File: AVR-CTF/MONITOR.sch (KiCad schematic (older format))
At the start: 13 parts

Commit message: Esquematico para revision
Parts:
- gave numbers to parts that had none: 13
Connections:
- net VDD renamed +3V3
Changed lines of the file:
@@
 $EndDescr
 $Comp
-L RF_Module:ESP32-WROOM-32D U?
+L RF_Module:ESP32-WROOM-32D U3
 U 1 1 621CC162
 P 1800 2350
-F 0 "U?" H 2300 900 50  0000 C CNN
+F 0 "U3" H 2300 900 50  0000 C CNN
 F 1 "ESP32-WROOM-32D" H 2300 1000 50  0000 C CNN
 F 2 "RF_Module:ESP32-WROOM-32" H 1800 850 50  0001 C CNN
@@
 $EndComp
 $Comp
-L Device:C C?
+L Device:C C6
 U 1 1 621D2118
 P 3400 950
-F 0 "C?" H 3515 996 50  0000 L CNN
+F 0 "C6" H 3515 996 50  0000 L CNN
 F 1 "10uF" H 3515 905 50  0000 L CNN
 F 2 "Capacitor_SMD:C_0805_2012Metric_Pad1.18x1.45mm_HandSolder" H 3438 800 50  0001 C CNN
@@
 $EndComp
 $Comp
-L Device:C C?
+L Device:C C7
 U 1 1 621D24F4
 P 3800 950
-F 0 "C?" H 3915 996 50  0000 L CNN
+F 0 "C7" H 3915 996 50  0000 L CNN
 F 1 "1uF" H 3915 905 50  0000 L CNN
 F 2 "Capacitor_SMD:C_0603_1608Metric_Pad1.08x0.95mm_HandSolder" H 3838 800 50  0001 C CNN
@@
 $EndComp
 $Comp
-L Device:C C?
+L Device:C C8
 U 1 1 621D2B1C
 P 4200 950
-F 0 "C?" H 4315 996 50  0000 L CNN
+F 0 "C8" H 4315 996 50  0000 L CNN
 F 1 "0.1uF" H 4315 905 50  0000 L CNN
 F 2 "Capacitor_SMD:C_0603_1608Metric_Pad1.08x0.95mm_HandSolder" H 4238 800 50  0001 C CNN
@@
 	3800 1100 4200 1100
 Connection ~ 3800 1100
-$Comp
-L power:VDD #PWR?
-U 1 1 621E240B
-P 3800 800
-F 0 "#PWR?" H 3800 650 50  0001 C CNN
-F 1 "VDD" H 3815 973 50  0000 C CNN
-F 2 "" H 3800 800 50  0001 C CNN
-F 3 "" H 3800 800 50  0001 C CNN
-	1    3800 800
-	1    0    0    -1
-$EndComp
-$Comp
-L power:VDD #PWR?
-U 1 1 621E27EB
-P 1800 900
-F 0 "#PWR?" H 1800 750 50  0001 C CNN
-F 1 "VDD" H 1815 1073 50  0000 C CNN
-F 2 "" H 1800 900 50  0001 C CNN
-F 3 "" H 1800 900 50  0001 C CNN
-	1    1800 900
-	1    0    0    -1
-$EndComp
 Wire Wire Line
 	1800 900  1800 950
 $Comp
-L power:GND #PWR?
+L power:GND #PWR017
 U 1 1 621E322C
 P 3800 1200
-F 0 "#PWR?" H 3800 950 50  0001 C CNN
+F 0 "#PWR017" H 3800 950 50  0001 C CNN
 F 1 "GND" H 3805 1027 50  0000 C CNN
 F 2 "" H 3800 1200 50  0001 C CNN
@@
 	3800 1100 3800 1200
 $Comp
-L power:GND #PWR?
+L power:GND #PWR014
 U 1 1 621E3647
 P 1800 3750
-F 0 "#PWR?" H 1800 3500 50  0001 C CNN
+F 0 "#PWR014" H 1800 3500 50  0001 C CNN
 F 1 "GND" H 1805 3577 50  0000 C CNN
 F 2 "" H 1800 3750 50  0001 C CNN
@@
 $EndComp
 $Comp
-L Device:R R?
+L Device:R R4
 U 1 1 621E4581
 P 5775 975
-F 0 "R?" H 5845 1021 50  0000 L CNN
+F 0 "R4" H 5845 1021 50  0000 L CNN
 F 1 "10K" H 5845 930 50  0000 L CNN
 F 2 "Resistor_SMD:R_0603_1608Metric_Pad0.98x0.95mm_HandSolder" V 5705 975 50  0001 C CNN
@@
 $EndComp
 $Comp
-L Device:C C?
+L Device:C C9
 U 1 1 621E49B9
 P 5775 1325
-F 0 "C?" H 5890 1371 50  0000 L CNN
+F 0 "C9" H 5890 1371 50  0000 L CNN
 F 1 "0.1uF" H 5890 1280 50  0000 L CNN
 F 2 "Capacitor_SMD:C_0603_1608Metric_Pad1.08x0.95mm_HandSolder" H 5813 1175 50  0001 C CNN
@@
 $EndComp
 $Comp
-L power:GND #PWR?
+L power:GND #PWR019
 U 1 1 621E4F01
 P 5775 1525
-F 0 "#PWR?" H 5775 1275 50  0001 C CNN
+F 0 "#PWR019" H 5775 1275 50  0001 C CNN
 F 1 "GND" H 5780 1352 50  0000 C CNN
 F 2 "" H 5775 1525 50  0001 C CNN
 F 3 "" H 5775 1525 50  0001 C CNN
 	1    5775 1525
-	1    0    0    -1
-$EndComp
-$Comp
-L power:VDD #PWR?
-U 1 1 621E53C7
-P 5775 775
-F 0 "#PWR?" H 5775 625 50  0001 C CNN
-F 1 "VDD" H 5790 948 50  0000 C CNN
-F 2 "" H 5775 775 50  0001 C CNN
-F 3 "" H 5775 775 50  0001 C CNN
-	1    5775 775
 	1    0    0    -1
 $EndComp
@@
 NoConn ~ 2400 2950
 $Comp
-L Device:R R?
+L Device:R R2
 U 1 1 6217A167
 P 1500 5500
-F 0 "R?" H 1570 5546 50  0000 L CNN
+F 0 "R2" H 1570 5546 50  0000 L CNN
 F 1 "10K" H 1570 5455 50  0000 L CNN
 F 2 "Resistor_SMD:R_0603_1608Metric_Pad0.98x0.95mm_HandSolder" V 1430 5500 50  0001 C CNN
@@
 	1500 5650 1725 5650
 $Comp
-L Device:R R?
+L Device:R R3
 U 1 1 6217B155
 P 1500 5925
-F 0 "R?" H 1325 5950 50  0000 L CNN
+F 0 "R3" H 1325 5950 50  0000 L CNN
 F 1 "10K" H 1300 5875 50  0000 L CNN
 F 2 "Resistor_SMD:R_0603_1608Metric_Pad0.98x0.95mm_HandSolder" V 1430 5925 50  0001 C CNN
@@
 	1500 5650 1250 5650
 Connection ~ 1500 5650
-$Comp
-L power:VDD #PWR?
-U 1 1 6217E4A0
-P 1500 5350
-F 0 "#PWR?" H 1500 5200 50  0001 C CNN
-F 1 "VDD" H 1515 5523 50  0000 C CNN
-F 2 "" H 1500 5350 50  0001 C CNN
-F 3 "" H 1500 5350 50  0001 C CNN
-	1    1500 5350
-	1    0    0    -1
-$EndComp
-$Comp
-L power:VDD #PWR?
-U 1 1 6217EDA0
-P 1500 6075
-F 0 "#PWR?" H 1500 5925 50  0001 C CNN
-F 1 "VDD" H 1515 6248 50  0000 C CNN
-F 2 "" H 1500 6075 50  0001 C CNN
-F 3 "" H 1500 6075 50  0001 C CNN
-	1    1500 6075
-	-1   0    0    1
-$EndComp
 Text Notes 1500 4150 0    62   ~ 0
 PROGRAMMING
@@
 EN
 $Comp
-L Device:R R?
+L Device:R R5
 U 1 1 62117B24
 P 5775 2300
-F 0 "R?" H 5845 2346 50  0000 L CNN
+F 0 "R5" H 5845 2346 50  0000 L CNN
 F 1 "10K" H 5845 2255 50  0000 L CNN
 F 2 "Resistor_SMD:R_0603_1608Metric_Pad0.98x0.95mm_HandSolder" V 5705 2300 50  0001 C CNN
@@
 $EndComp
 $Comp
-L Device:C C?
+L Device:C C10
 U 1 1 62117B2A
 P 5775 2650
-F 0 "C?" H 5890 2696 50  0000 L CNN
+F 0 "C10" H 5890 2696 50  0000 L CNN
 F 1 "0.1uF" H 5890 2605 50  0000 L CNN
 F 2 "Capacitor_SMD:C_0603_1608Metric_Pad1.08x0.95mm_HandSolder" H 5813 2500 50  0001 C CNN
@@
 $EndComp
 $Comp
-L power:GND #PWR?
+L power:GND #PWR021
 U 1 1 62117B30
 P 5775 2850
-F 0 "#PWR?" H 5775 2600 50  0001 C CNN
+F 0 "#PWR021" H 5775 2600 50  0001 C CNN
 F 1 "GND" H 5780 2677 50  0000 C CNN
 F 2 "" H 5775 2850 50  0001 C CNN
@@
 	1    0    0    -1
 $EndComp
-$Comp
-L power:VDD #PWR?
-U 1 1 62117B36
-P 5775 2100
-F 0 "#PWR?" H 5775 1950 50  0001 C CNN
-F 1 "VDD" H 5790 2273 50  0000 C CNN
-F 2 "" H 5775 2100 50  0001 C CNN
-F 3 "" H 5775 2100 50  0001 C CNN
-	1    5775 2100
-	1    0    0    -1
-$EndComp
 Wire Wire Line
 	4850 2925 4850 3000
@@
 BOOT
 $Comp
-L Connector_Generic:Conn_01x04 J?
+L Connector_Generic:Conn_01x04 J3
 U 1 1 625AE0CF
 P 1750 4625
-F 0 "J?" H 1668 4200 50  0000 C CNN
+F 0 "J3" H 1668 4200 50  0000 C CNN
 F 1 "Prog" H 1668 4291 50  0000 C CNN
 F 2 "Connector_PinHeader_2.54mm:PinHeader_1x04_P2.54mm_Vertical" H 1750 4625 50  0001 C CNN
@@
 U0-TX
 $Comp
-L power:GND #PWR?
+L power:GND #PWR015
 U 1 1 625B38C3
 P 2000 4775
-F 0 "#PWR?" H 2000 4525 50  0001 C CNN
+F 0 "#PWR015" H 2000 4525 50  0001 C CNN
 F 1 "GND" H 2005 4602 50  0000 C CNN
 F 2 "" H 2000 4775 50  0001 C CNN
@@
 NoConn ~ 1950 4425
 $Comp
-L AVR-CTF-symbols:4-1437565-2 SW?
+L AVR-CTF-symbols:4-1437565-2 SW1
 U 1 1 621FE361
 P 4950 1350
-F 0 "SW?" V 4904 1528 50  0000 L CNN
+F 0 "SW1" V 4904 1528 50  0000 L CNN
 F 1 "4-1437565-2" V 4995 1528 50  0000 L CNN
 F 2 "AVR-CTF-footprints:Push_button_FSM4JSMATR" H 4950 1350 50  0001 L BNN
@@
 $EndComp
 $Comp
-L AVR-CTF-symbols:4-1437565-2 SW?
+L AVR-CTF-symbols:4-1437565-2 SW2
 U 1 1 622014F9
 P 4950 2675
-F 0 "SW?" V 4904 2853 50  0000 L CNN
+F 0 "SW2" V 4904 2853 50  0000 L CNN
 F 1 "4-1437565-2" V 4995 2853 50  0000 L CNN
 F 2 "AVR-CTF-footprints:Push_button_FSM4JSMATR" H 4950 2675 50  0001 L BNN
@@
 	0    1    1    0
 $EndComp
+Text Label 2500 2150 0    50   ~ 0
+U2_RX
+Text Label 2500 2250 0    50   ~ 0
+U2_TX
+$Comp
+L power:+3.3V #PWR?
+U 1 1 6274E363
+P 1800 900
+AR Path="/621FA25F/6274E363" Ref="#PWR?"  Part="1"
+AR Path="/621FB334/6274E363" Ref="#PWR0101"  Part="1"
+F 0 "#PWR0101" H 1800 750 50  0001 C CNN
+F 1 "+3.3V" H 1815 1073 50  0000 C CNN
+F 2 "" H 1800 900 50  0001 C CNN
+F 3 "" H 1800 900 50  0001 C CNN
+	1    1800 900
+	1    0    0    -1
+$EndComp
+$Comp
+L power:+3.3V #PWR?
+U 1 1 6274F33F
+P 3800 800
+AR Path="/621FA25F/6274F33F" Ref="#PWR?"  Part="1"
+AR Path="/621FB334/6274F33F" Ref="#PWR0102"  Part="1"
+F 0 "#PWR0102" H 3800 650 50  0001 C CNN
+F 1 "+3.3V" H 3815 973 50  0000 C CNN
+F 2 "" H 3800 800 50  0001 C CNN
+F 3 "" H 3800 800 50  0001 C CNN
+	1    3800 800
+	1    0    0    -1
+$EndComp
+$Comp
+L power:+3.3V #PWR?
+U 1 1 6274F774
+P 5775 775
+AR Path="/621FA25F/6274F774" Ref="#PWR?"  Part="1"
+AR Path="/621FB334/6274F774" Ref="#PWR0103"  Part="1"
+F 0 "#PWR0103" H 5775 625 50  0001 C CNN
+F 1 "+3.3V" H 5790 948 50  0000 C CNN
+F 2 "" H 5775 775 50  0001 C CNN
+F 3 "" H 5775 775 50  0001 C CNN
+	1    5775 775
+	1    0    0    -1
+$EndComp
+$Comp
+L power:+3.3V #PWR?
+U 1 1 6274FF68
+P 5775 2100
+AR Path="/621FA25F/6274FF68" Ref="#PWR?"  Part="1"
+AR Path="/621FB334/6274FF68" Ref="#PWR0104"  Part="1"
+F 0 "#PWR0104" H 5775 1950 50  0001 C CNN
+F 1 "+3.3V" H 5790 2273 50  0000 C CNN
+F 2 "" H 5775 2100 50  0001 C CNN
+F 3 "" H 5775 2100 50  0001 C CNN
+	1    5775 2100
+	1    0    0    -1
+$EndComp
+$Comp
+L power:+3.3V #PWR?
+U 1 1 6275236D
+P 1500 5350
+AR Path="/621FA25F/6275236D" Ref="#PWR?"  Part="1"
+AR Path="/621FB334/6275236D" Ref="#PWR0106"  Part="1"
+F 0 "#PWR0106" H 1500 5200 50  0001 C CNN
+F 1 "+3.3V" H 1515 5523 50  0000 C CNN
+F 2 "" H 1500 5350 50  0001 C CNN
+F 3 "" H 1500 5350 50  0001 C CNN
+	1    1500 5350
+	1    0    0    -1
+$EndComp
+$Comp
+L power:+3.3V #PWR?
+U 1 1 62752CBD
+P 1500 6075
+AR Path="/621FA25F/62752CBD" Ref="#PWR?"  Part="1"
+AR Path="/621FB334/62752CBD" Ref="#PWR0107"  Part="1"
+F 0 "#PWR0107" H 1500 5925 50  0001 C CNN
+F 1 "+3.3V" H 1515 6248 50  0000 C CNN
+F 2 "" H 1500 6075 50  0001 C CNN
+F 3 "" H 1500 6075 50  0001 C CNN
+	1    1500 6075
+	-1   0    0    1
+$EndComp
 $EndSCHEMATC

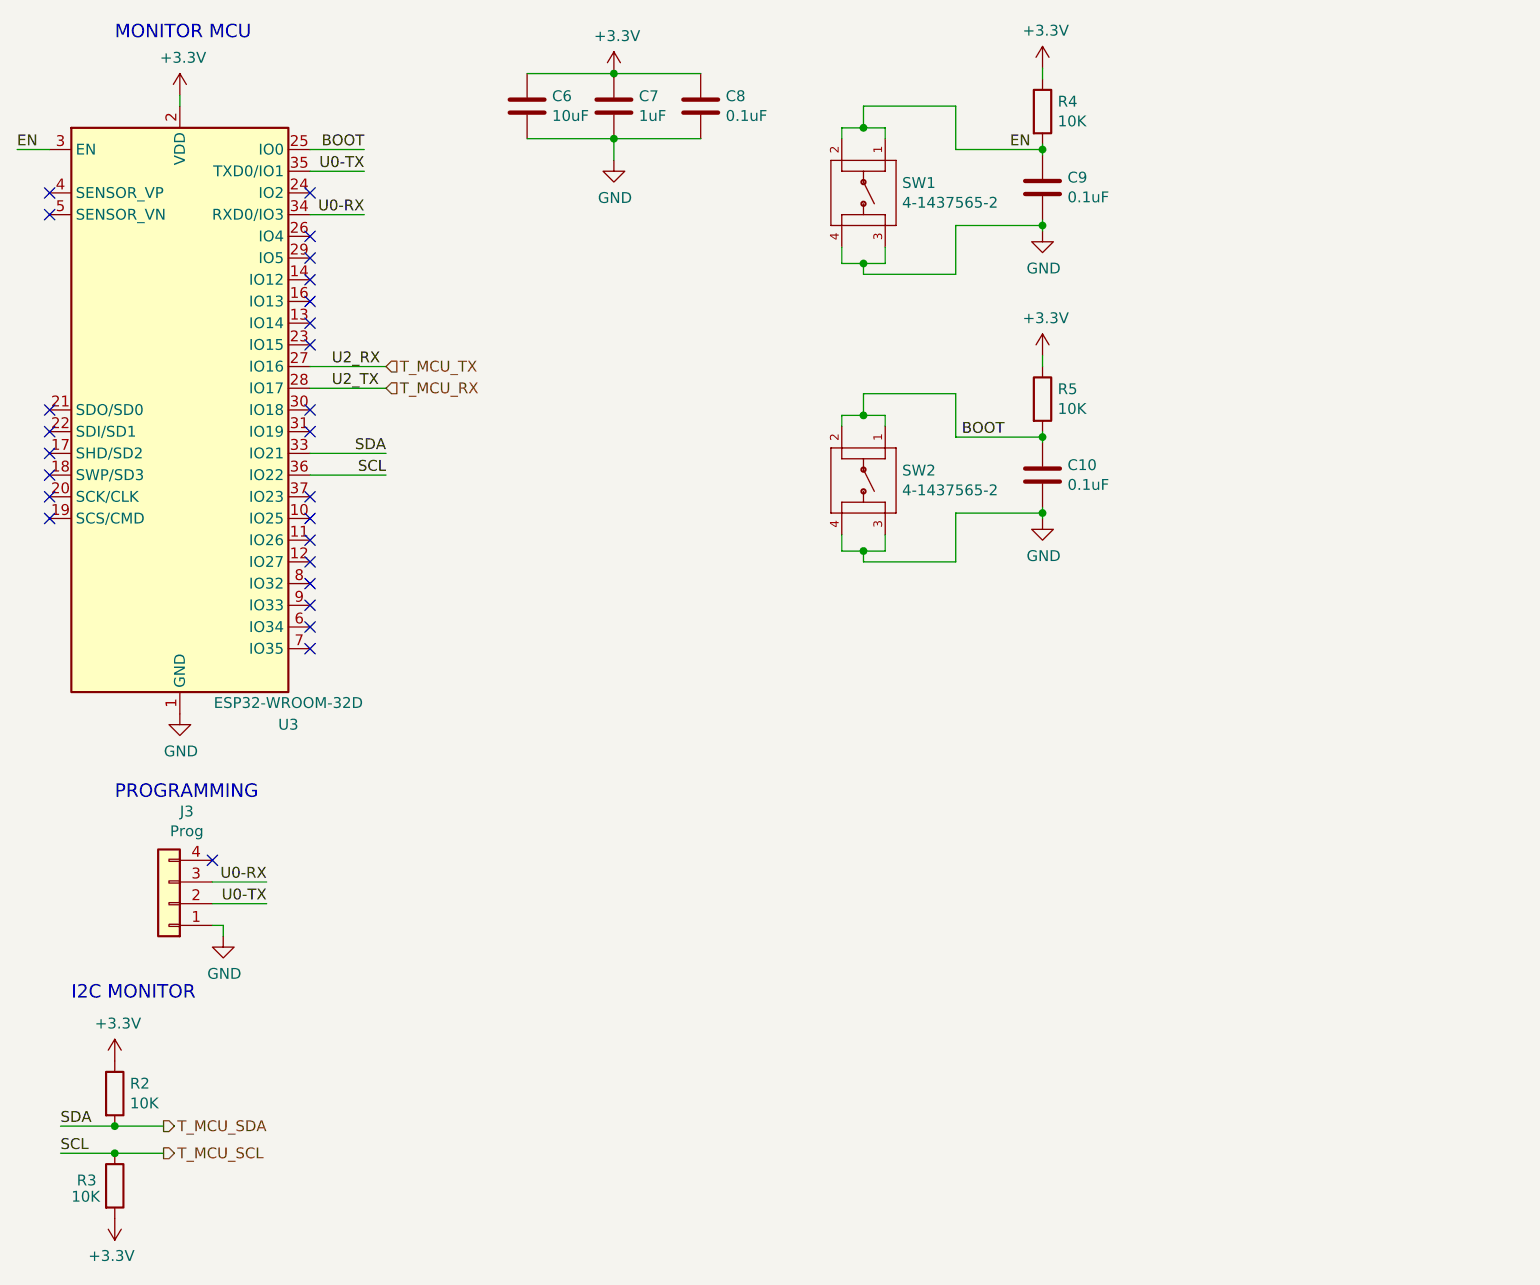
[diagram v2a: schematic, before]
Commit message: Anexo de otro FTDI y regulador de voltaje
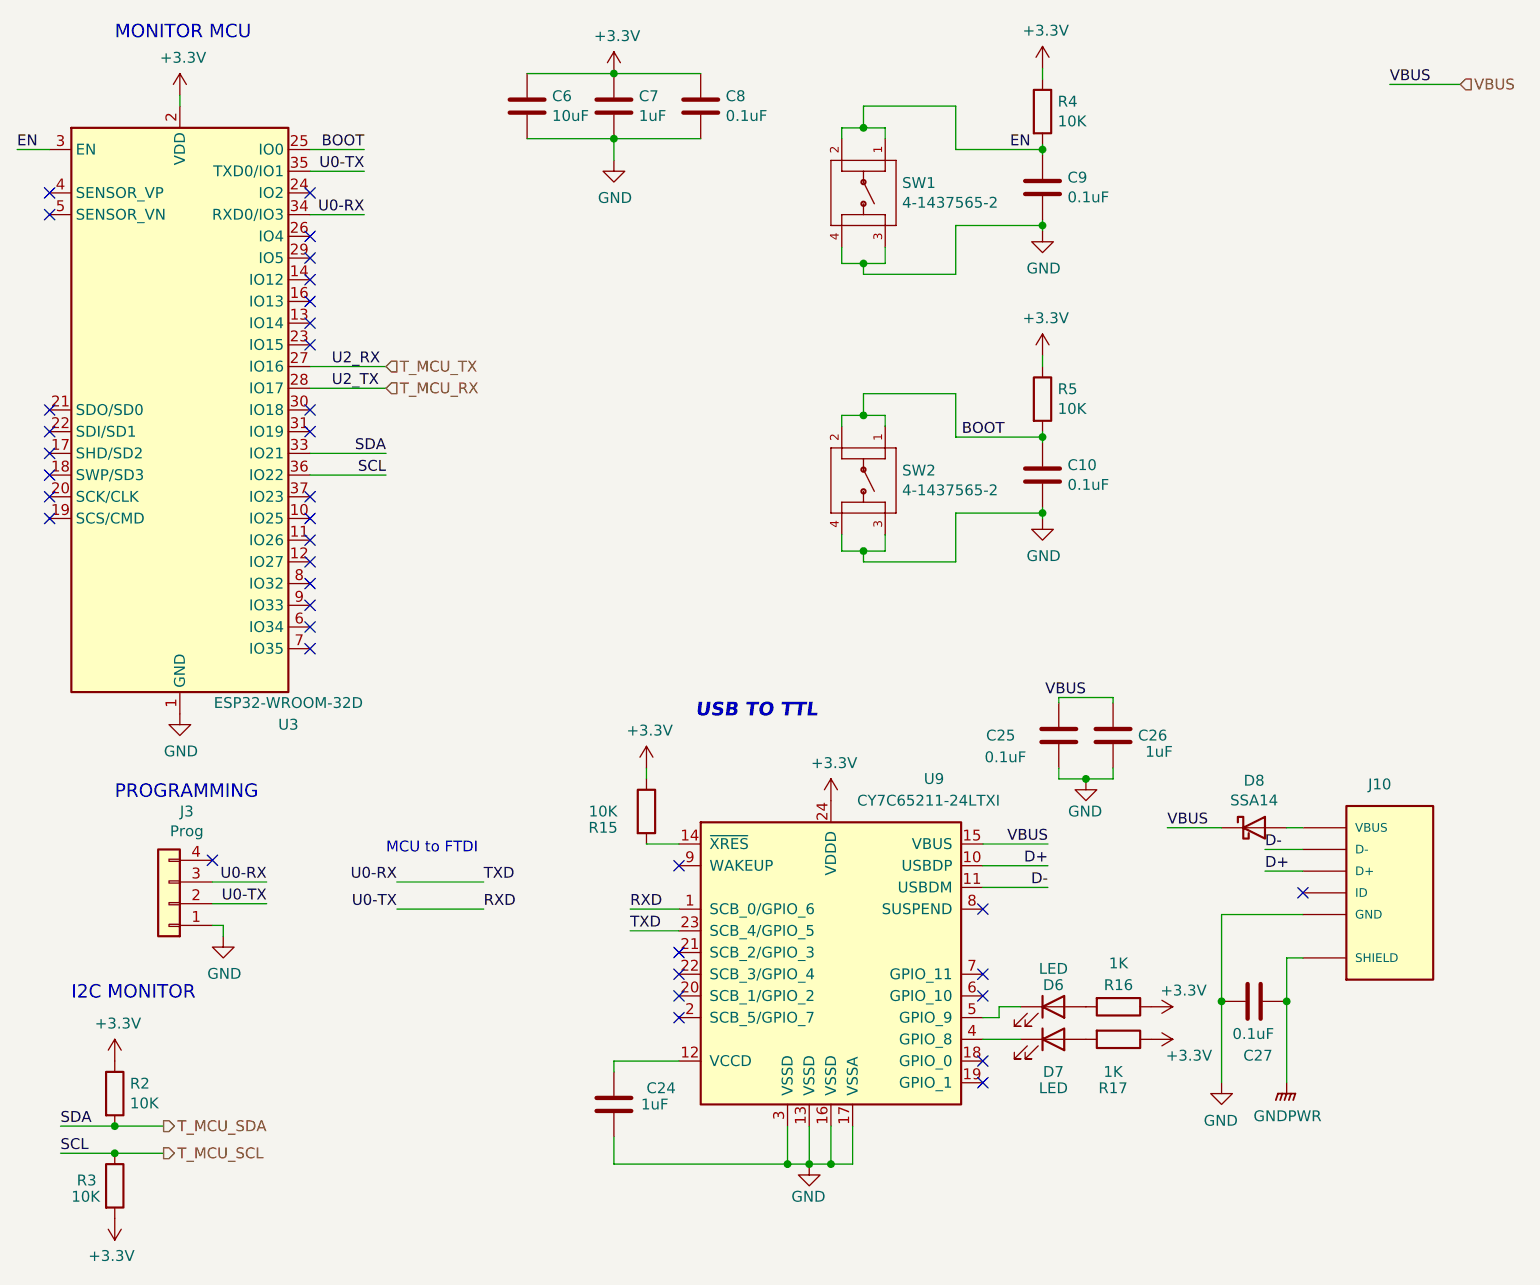
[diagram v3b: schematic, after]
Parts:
- added C24, C26: 1uF, Capacitor_SMD:C_0603_1608Metric_Pad1.08x0.95mm_HandSolder, symbol Device:C
- added C25, C27: 0.1uF, Capacitor_SMD:C_0603_1608Metric_Pad1.08x0.95mm_HandSolder, symbol Device:C
- added D6, D7: LED, LED_SMD:LED_0603_1608Metric_Pad1.05x0.95mm_HandSolder, symbol Device:LED
- added D8: SSA14, Diode_SMD:D_SMA_Handsoldering, symbol Device:D_Schottky
- added J10: USB3090-XX-X_REVE, GCT_USB3090-XX-X_REVE, symbol AVR-CTF-symbols:USB3090-XX-X_REVE
- added R15: 10K, Resistor_SMD:R_0603_1608Metric_Pad0.98x0.95mm_HandSolder, symbol Device:R
- added R16, R17: 1K, Resistor_SMD:R_0603_1608Metric_Pad0.98x0.95mm_HandSolder, symbol Device:R
- added U9: CY7C65211-24LTXI, Package_DFN_QFN:QFN-24-1EP_4x4mm_P0.5mm_EP2.6x2.6mm, symbol Interface_USB:CY7C65211-24LTXI
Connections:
- net +3V3: now also R15.1, R16.1, R17.1, U9.24 (VDDD)
- net GND: now also C24.2, C25.1, C26.1, C27.2, J10.5 (GND), U9.13 (VSSD), U9.16 (VSSD), U9.17 (VSSA), U9.3 (VSSD)
- net U0-RX renamed TXD
- net TXD: now also U9.23 (SCB_4/GPIO_5)
- net U0-TX renamed RXD
- net RXD: now also U9.1 (SCB_0/GPIO_6)
- new net: C24.1, U9.12 (VCCD)
- new net: R15.2, U9.14 (~XRES)
- new net: D7.1 (K), U9.4 (GPIO_8)
- new net: D6.1 (K), U9.5 (GPIO_9)
- new net: D8.2 (A), J10.1 (VBUS)
- new net: D7.2 (A), R17.2
- new net: D6.2 (A), R16.2
- new net D+: J10.3 (D+), U9.10 (USBDP)
- new net D-: J10.2 (D-), U9.11 (USBDM)
- new net GNDPWR: C27.1, J10.6 (SHIELD), J10.7 (SHIELD), J10.8 (SHIELD), J10.9 (SHIELD)
- new net VBUS: C25.2, C26.2, D8.1 (K), U9.15 (VBUS)
- no-connect marks 26 -> 37
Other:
- note added: "MCU to FTDI"
- note added: "USB TO TTL"

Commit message: Versión para revisión
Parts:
- J10: footprint GCT_USB3090-XX-X_REVE -> AVR-CTF-footprints:GCT_USB3090-XX-X_REVE
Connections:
- net GNDPWR renamed Earth
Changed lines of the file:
@@
 F 0 "J10" H 7275 5075 50  0000 L CNN
 F 1 "USB3090-XX-X_REVE" H 6800 5175 50  0001 L CNN
-F 2 "GCT_USB3090-XX-X_REVE" H 7375 4575 50  0001 L BNN
+F 2 "AVR-CTF-footprints:GCT_USB3090-XX-X_REVE" H 7375 4575 50  0001 L BNN
 F 3 "" H 7375 4575 50  0001 L BNN
 F 4 "GCT" H 7375 4575 50  0001 L BNN "MANUFACTURER"
@@
 F 3 "" H 6600 5450 50  0001 C CNN
 	1    6600 5450
-	1    0    0    -1
-$EndComp
-$Comp
-L power:GNDPWR #PWR?
-U 1 1 6230BCA5
-P 6900 5450
-AR Path="/6220499D/6230BCA5" Ref="#PWR?"  Part="1"
-AR Path="/621FB334/6230BCA5" Ref="#PWR060"  Part="1"
-F 0 "#PWR060" H 6900 5250 50  0001 C CNN
-F 1 "GNDPWR" H 6904 5296 50  0000 C CNN
-F 2 "" H 6900 5400 50  0001 C CNN
-F 3 "" H 6900 5400 50  0001 C CNN
-	1    6900 5450
 	1    0    0    -1
 $EndComp
@@
 Text Label 7375 850  0    50   ~ 0
 VBUS
+$Comp
+L power:Earth #PWR0108
+U 1 1 6239B255
+P 6900 5450
+F 0 "#PWR0108" H 6900 5200 50  0001 C CNN
+F 1 "Earth" H 6900 5300 50  0001 C CNN
+F 2 "" H 6900 5450 50  0001 C CNN
+F 3 "~" H 6900 5450 50  0001 C CNN
+	1    6900 5450
+	1    0    0    -1
+$EndComp
 $EndSCHEMATC

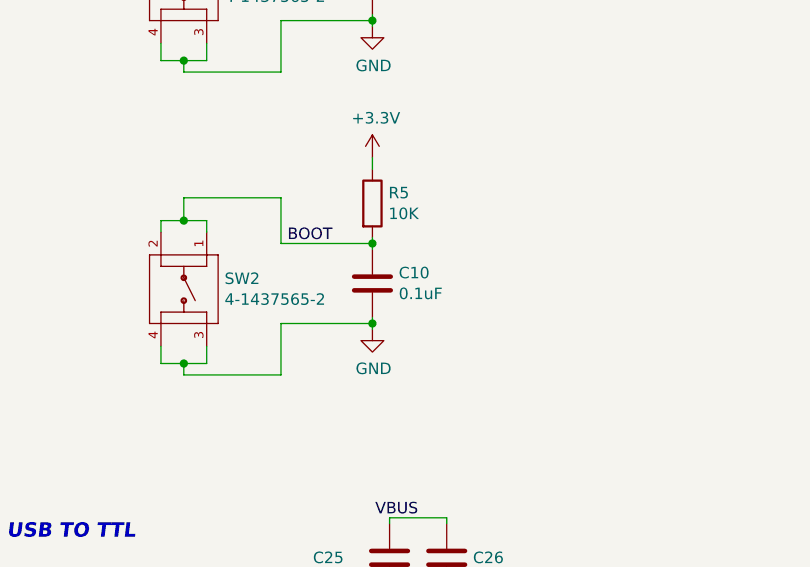
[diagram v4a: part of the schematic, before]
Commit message: Generacion de gerbers y boom agrupado
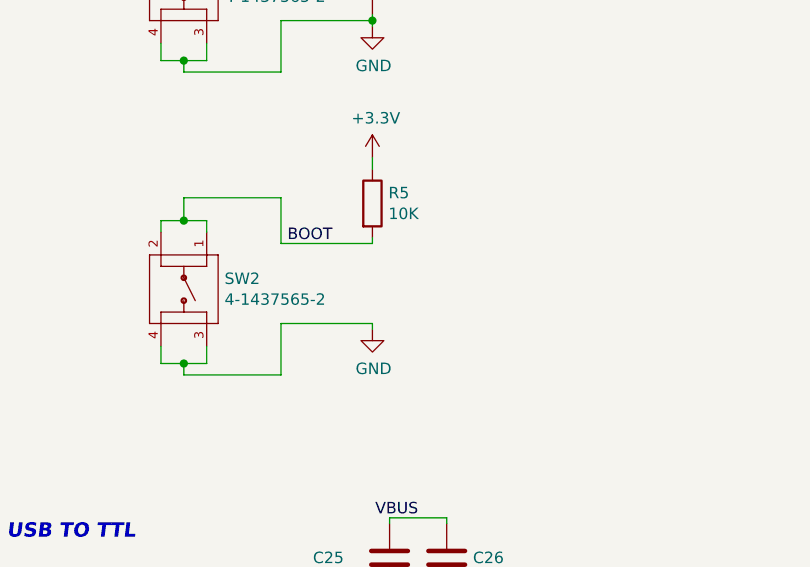
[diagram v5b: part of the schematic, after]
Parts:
- removed C10: 0.1uF, Capacitor_SMD:C_0603_1608Metric_Pad1.08x0.95mm_HandSolder, symbol Device:C
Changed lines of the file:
@@
-$EndComp
-$Comp
-L Device:C C10
-U 1 1 62117B2A
-P 5775 2650
-F 0 "C10" H 5890 2696 50  0000 L CNN
-F 1 "0.1uF" H 5890 2605 50  0000 L CNN
-F 2 "Capacitor_SMD:C_0603_1608Metric_Pad1.08x0.95mm_HandSolder" H 5813 2500 50  0001 C CNN
-F 3 "~" H 5775 2650 50  0001 C CNN
-	1    5775 2650
-	1    0    0    -1
 $EndComp
 $Comp
@@
 	5775 2450 5775 2475
 Wire Wire Line
-	5775 2800 5775 2825
-Wire Wire Line
 	5775 2475 5375 2475
 Wire Wire Line
@@
 Wire Wire Line
 	4950 2275 4950 2375
-Connection ~ 5775 2475
-Wire Wire Line
-	5775 2475 5775 2500
 Connection ~ 4950 2375
 Wire Wire Line
@@
 Wire Wire Line
 	4950 3000 5050 3000
-Connection ~ 5775 2825
 Wire Wire Line
 	5775 2825 5775 2850
